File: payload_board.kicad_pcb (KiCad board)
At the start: 4 copper layers, 100 x 100 mm, 100 parts, among them IC1 RP2040_QFN56, IC2 AZ1117CH-3.3TRG1, J1 Cam_PicoLock, J10 503398-1892, J12 FC Breakout, J15 SWC, J2 Cam_Conn, J3 Antenna_Conn, J4 usb jumper, J5 Display_Conn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

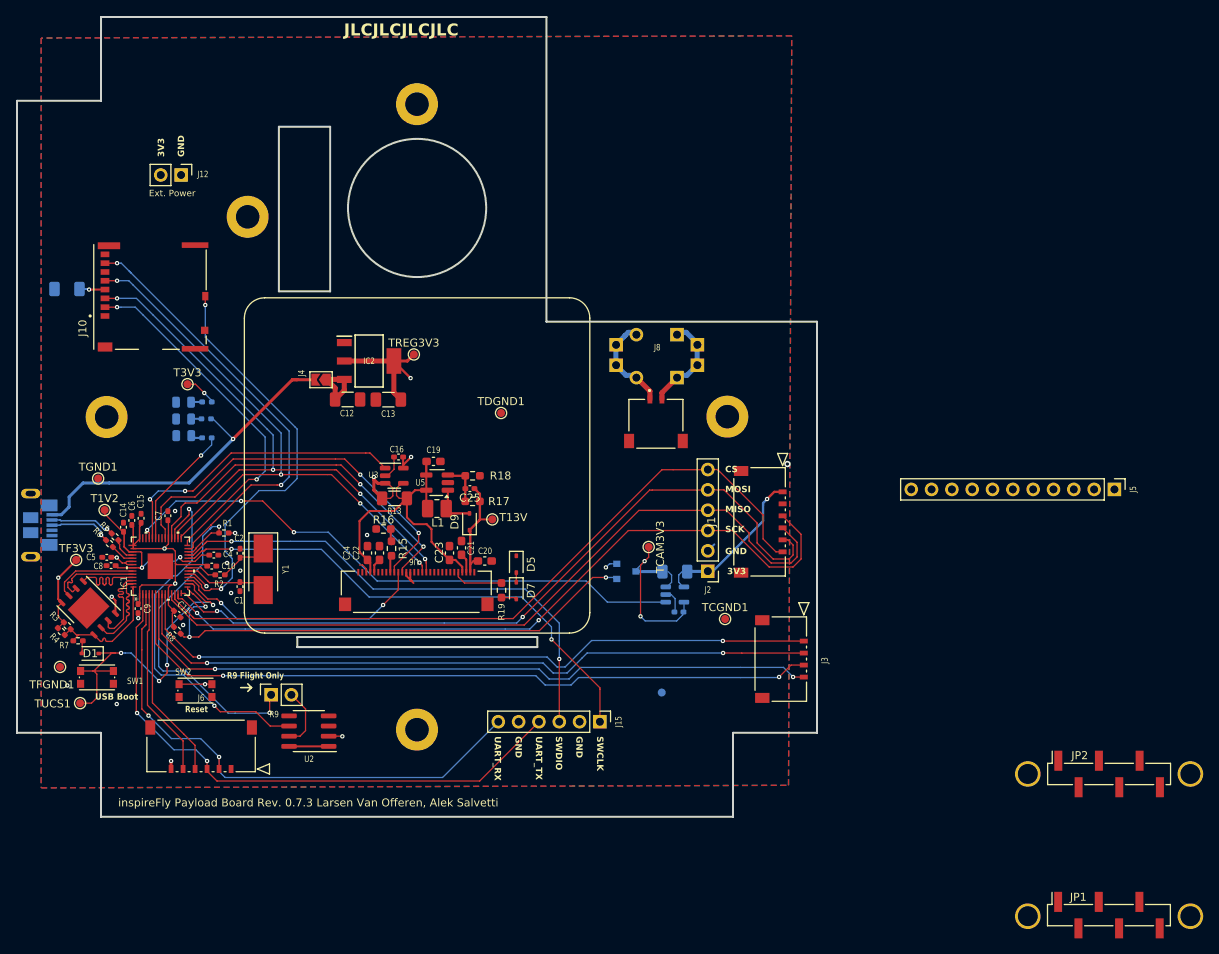
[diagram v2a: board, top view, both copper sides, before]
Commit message: Updated footprints to reduce part count.
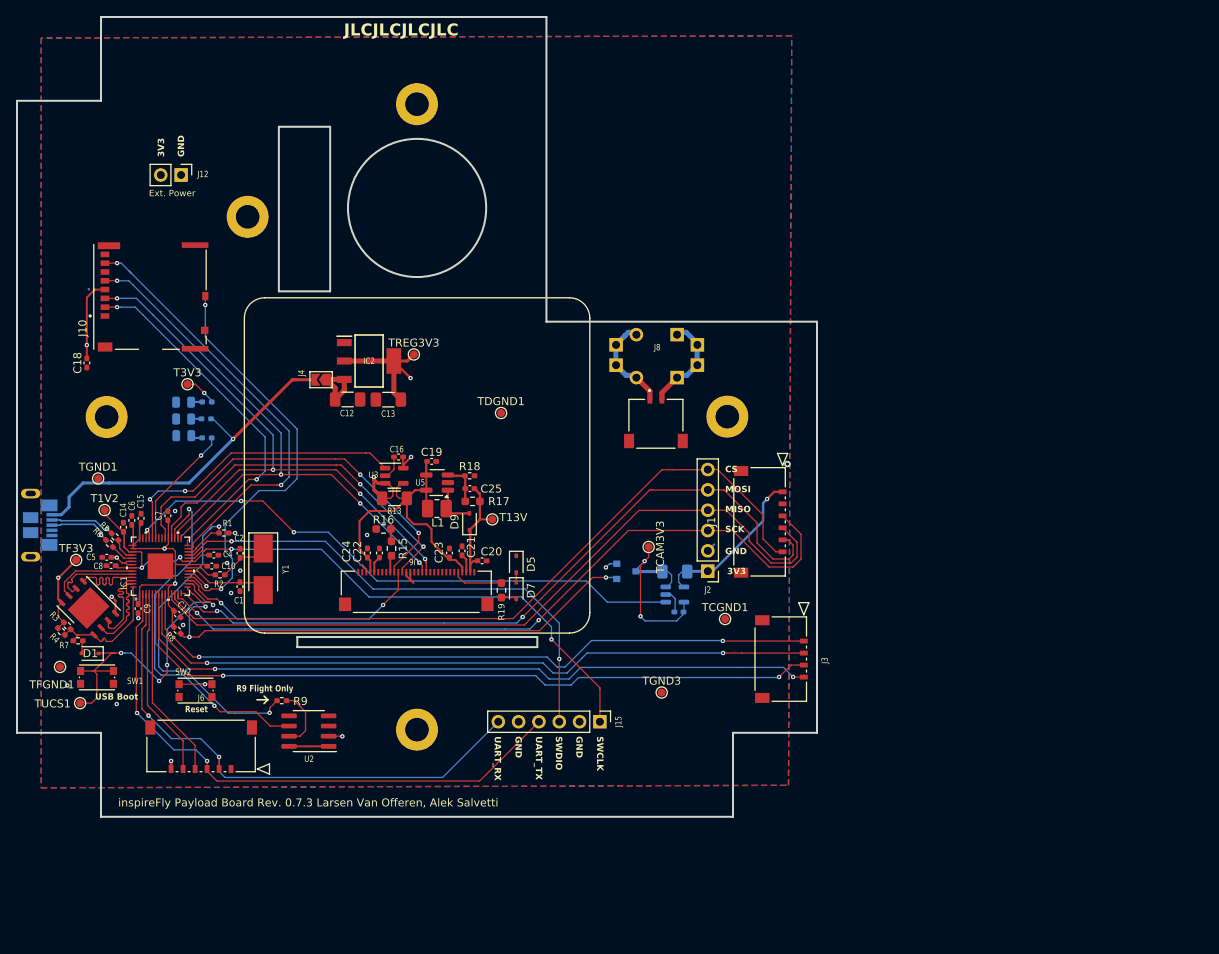
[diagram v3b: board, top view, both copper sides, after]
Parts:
- removed the ? at (159.7, 107.6)
- removed the ? at (139.3, 107.6)
- removed the ? at (159.7, 125.4)
- removed the ? at (139.3, 125.4)
- removed the J5 at (150.2, 72.0)
- removed JP1, JP2: , Connector_PinHeader_2.54mm:PinHeader_1x06_P2.54mm_Vertical_SMD_Pin1Right
- C18: footprint Capacitor_SMD:C_1206_3216Metric_Pad1.33x1.80mm_HandSolder -> Capacitor_SMD:C_0402_1005Metric_Pad0.74x0.62mm_HandSolder; moved to F.Cu
- C19, C20, C21, C24: footprint Capacitor_SMD:C_0603_1608Metric_Pad1.08x0.95mm_HandSolder -> Capacitor_SMD:C_0402_1005Metric_Pad0.74x0.62mm_HandSolder
- C22, C23: value 1.0uF -> 1uF; footprint Capacitor_SMD:C_0603_1608Metric_Pad1.08x0.95mm_HandSolder -> Capacitor_SMD:C_0402_1005Metric_Pad0.74x0.62mm_HandSolder
- R1: value 10K -> 10k
- R18: footprint Resistor_SMD:R_0603_1608Metric_Pad0.98x0.95mm_HandSolder -> Resistor_SMD:R_0402_1005Metric_Pad0.72x0.64mm_HandSolder
- R9: footprint Connector_PinSocket_2.54mm:PinSocket_1x02_P2.54mm_Vertical -> Resistor_SMD:R_0402_1005Metric_Pad0.72x0.64mm_HandSolder
- TGND3: moved to F.Cu
- moved C18 9.57 mm to (21.7, 56.2), turned to 90 degrees
- moved R9 1.53 mm to (46.1, 98.5), turned to 0 degrees
- moved C21 0.37 mm to (68.6, 79.7)
- moved R18 0.36 mm to (69.6, 70.3)
- moved C20 0.34 mm to (71.1, 81.0)
- moved C19 0.23 mm to (64.8, 68.5)
- turned TGND3 to 0 degrees
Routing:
- net +3.3V: track 92.3 -> 99.7 mm
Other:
- board text removed: "Keep Together. Mounting for IMU"

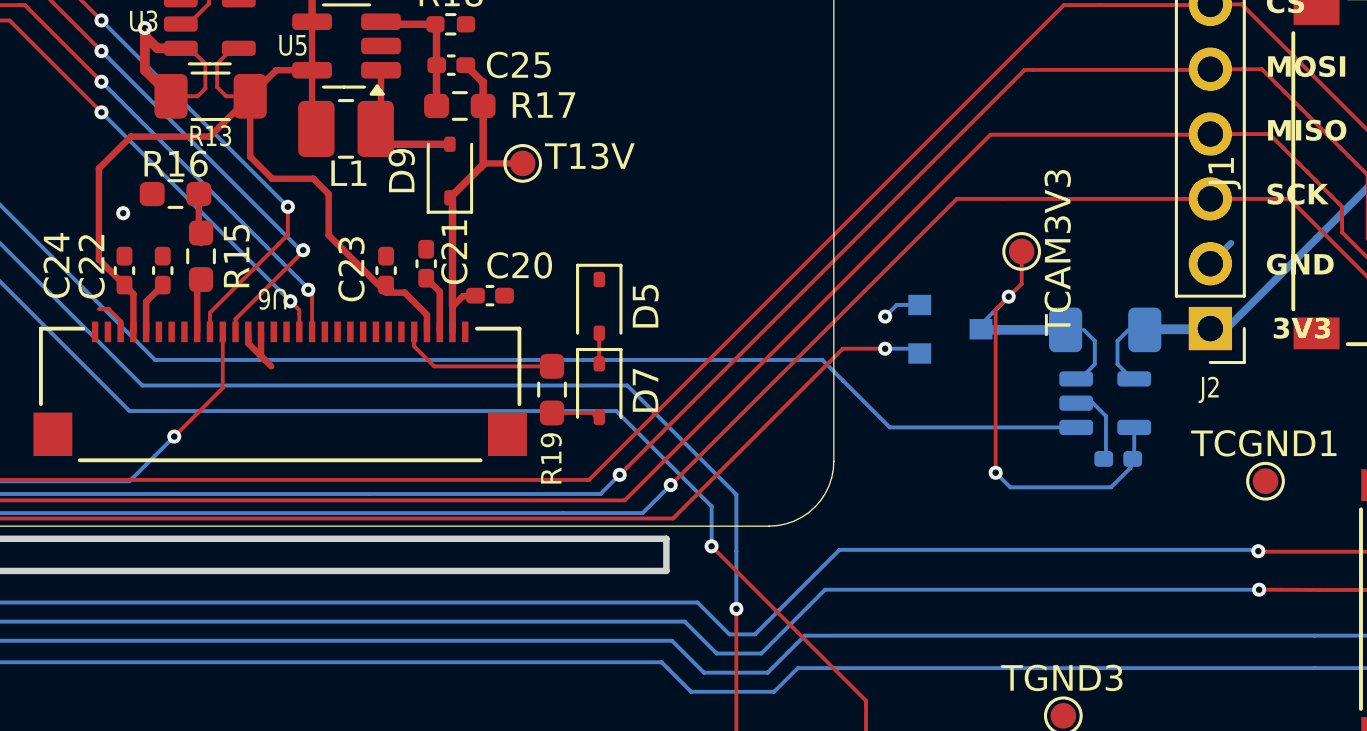
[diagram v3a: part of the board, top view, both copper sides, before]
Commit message: flipped camera power monitor and reset
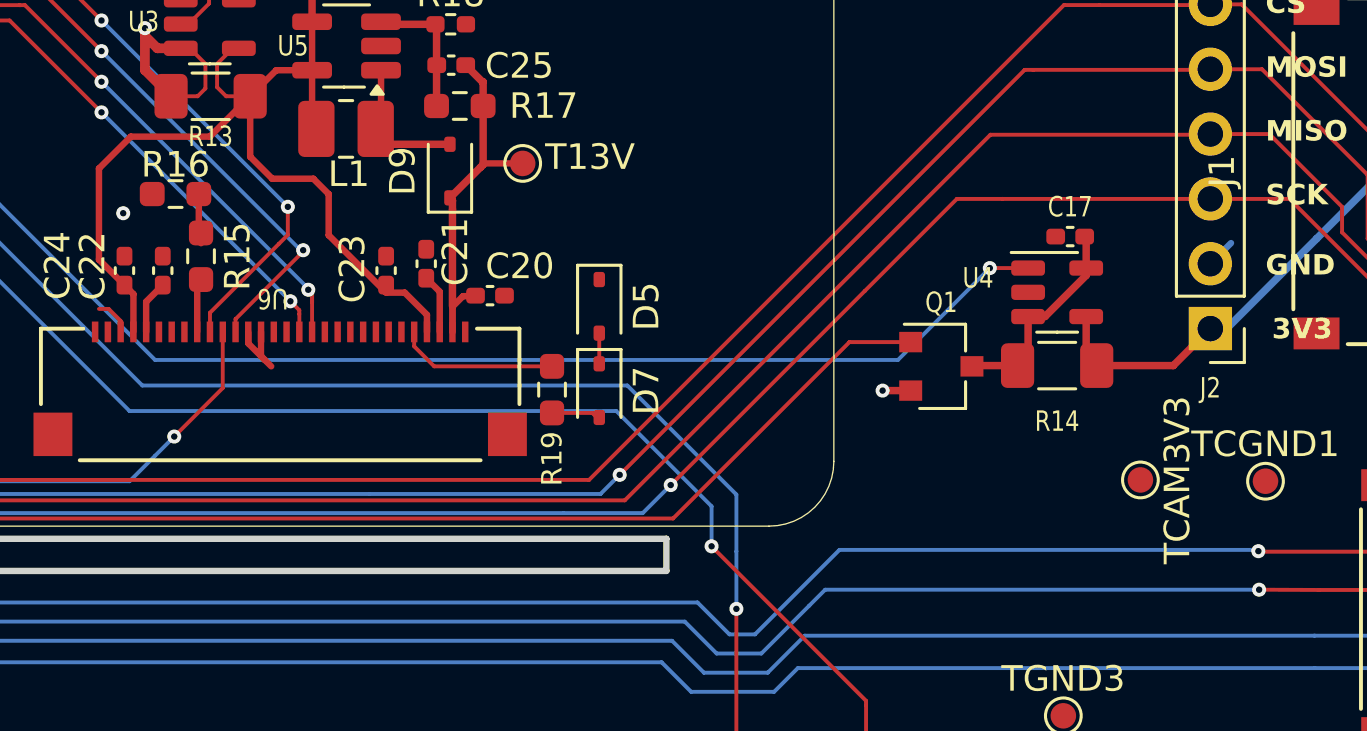
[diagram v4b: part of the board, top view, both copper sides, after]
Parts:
- C17, Q1, R14, U4: moved to F.Cu
- moved TCAM3V3 10.1 mm to (96.6, 88.2)
- moved C17 8.91 mm to (93.8, 78.7)
- moved U4 4.73 mm to (93.3, 80.8)
- moved R14 2.35 mm to (93.3, 83.7)
- moved Q1 1.50 mm to (88.8, 83.8)
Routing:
- net Cam_3.3v: track 23.8 -> 8.38 mm, vias 2 -> 0
- net GND: track 16.8 -> 13.8 mm
- net CIN-: track 19.4 -> 21.9 mm
- net ADC1: track 72.8 -> 71.3 mm, vias 3 -> 4
- net Cam_RST: track 66.8 -> 66.5 mm, vias 3 -> 2

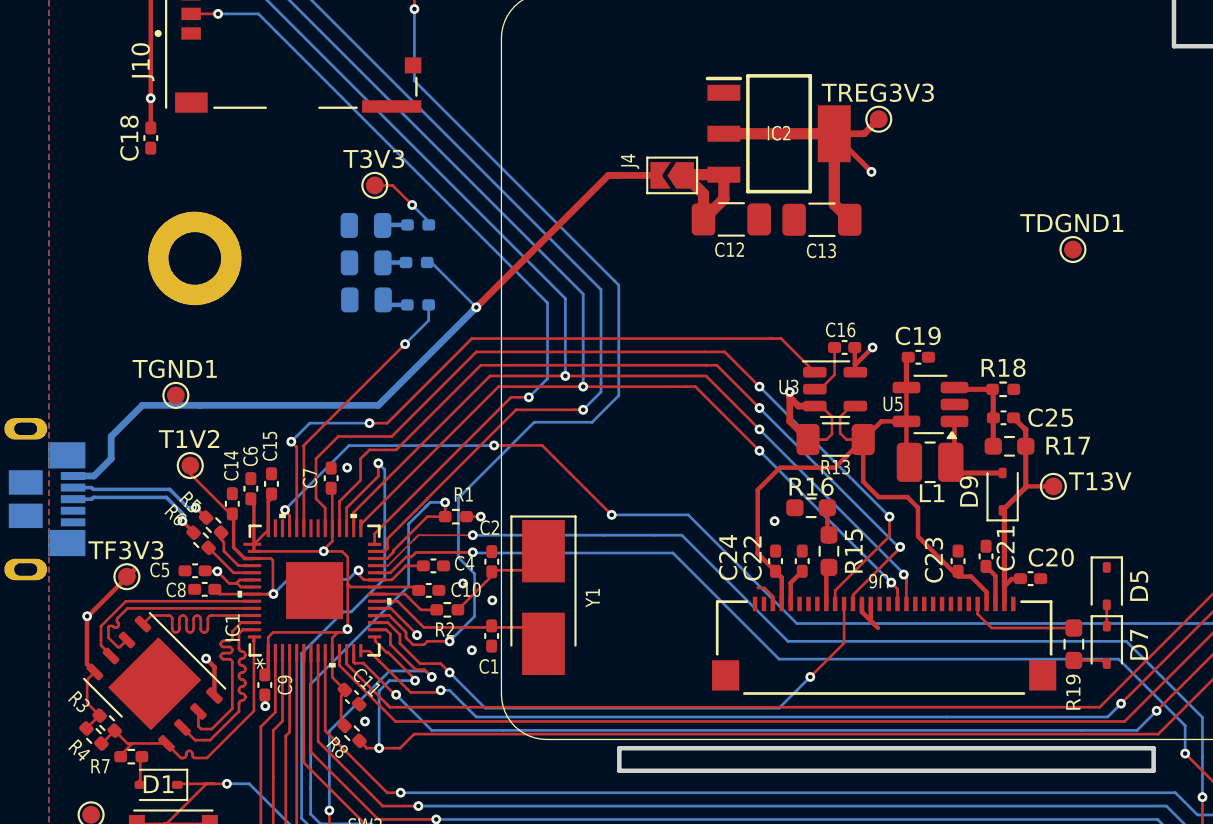
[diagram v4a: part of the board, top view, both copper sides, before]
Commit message: Update for JLC PCBA part selection
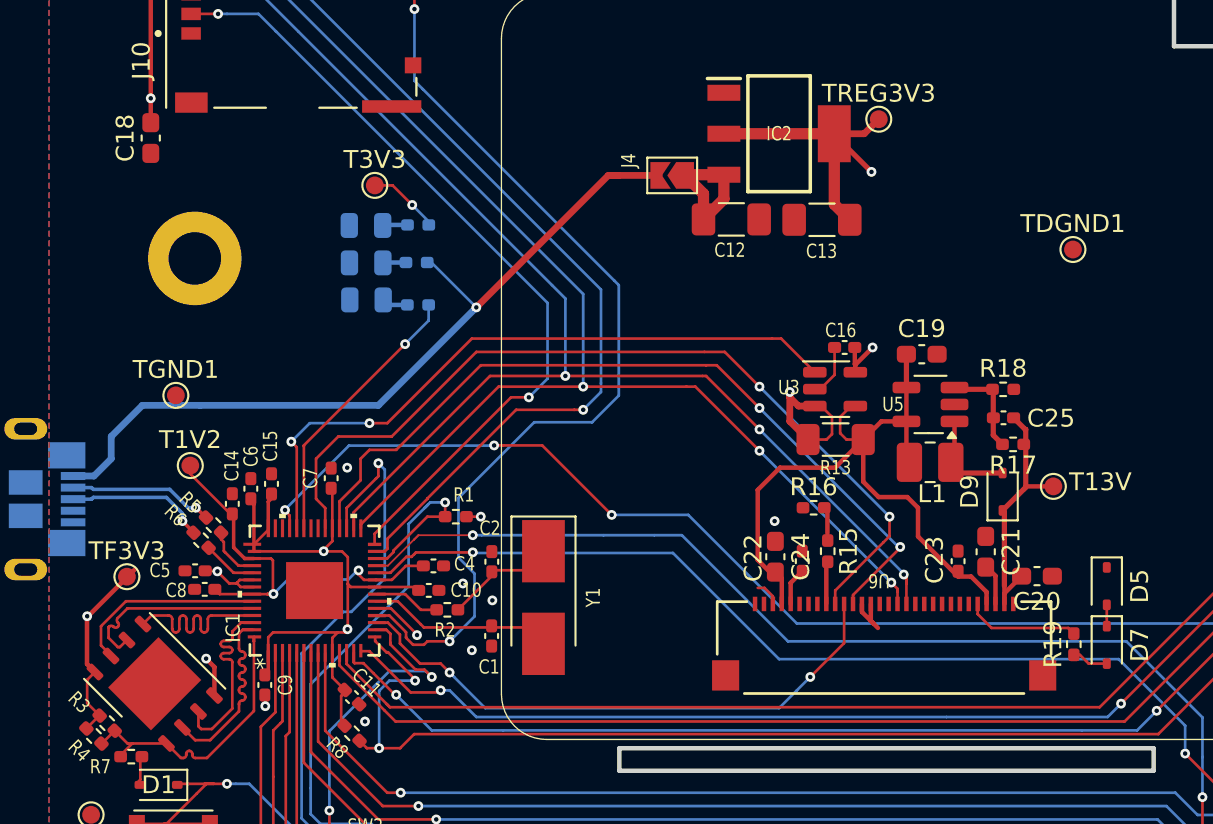
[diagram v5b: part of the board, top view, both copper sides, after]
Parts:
- C18, C19, C20, C21, C24: footprint Capacitor_SMD:C_0402_1005Metric_Pad0.74x0.62mm_HandSolder -> Capacitor_SMD:C_0603_1608Metric_Pad1.08x0.95mm_HandSolder
- R14: value 10k -> 0.065
- R15, R16, R17, R19: footprint Resistor_SMD:R_0603_1608Metric_Pad0.98x0.95mm_HandSolder -> Resistor_SMD:R_0402_1005Metric_Pad0.72x0.64mm_HandSolder
- moved C20 0.39 mm to (71.5, 80.8)
- moved C21 0.26 mm to (68.6, 79.5)
- moved C19 0.25 mm to (65.0, 68.4)
- moved C24 0.25 mm to (56.8, 79.8)
- moved R17 0.23 mm to (70.1, 73.4)
- moved R16 0.14 mm to (58.9, 77.0)
- moved R15 0.07 mm to (59.7, 79.4)
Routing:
- net DIN-: track 39.7 -> 40.3 mm

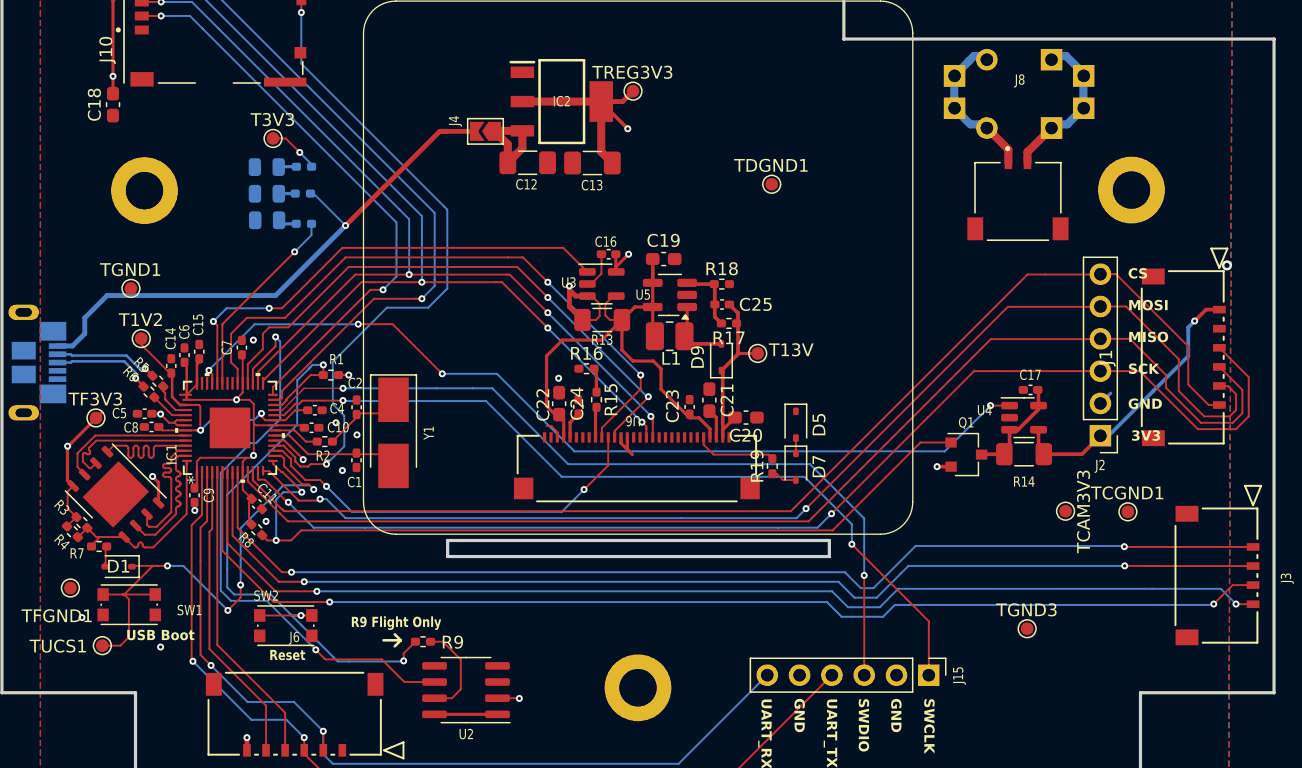
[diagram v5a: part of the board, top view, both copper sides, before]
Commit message: Added new 13V boost converter
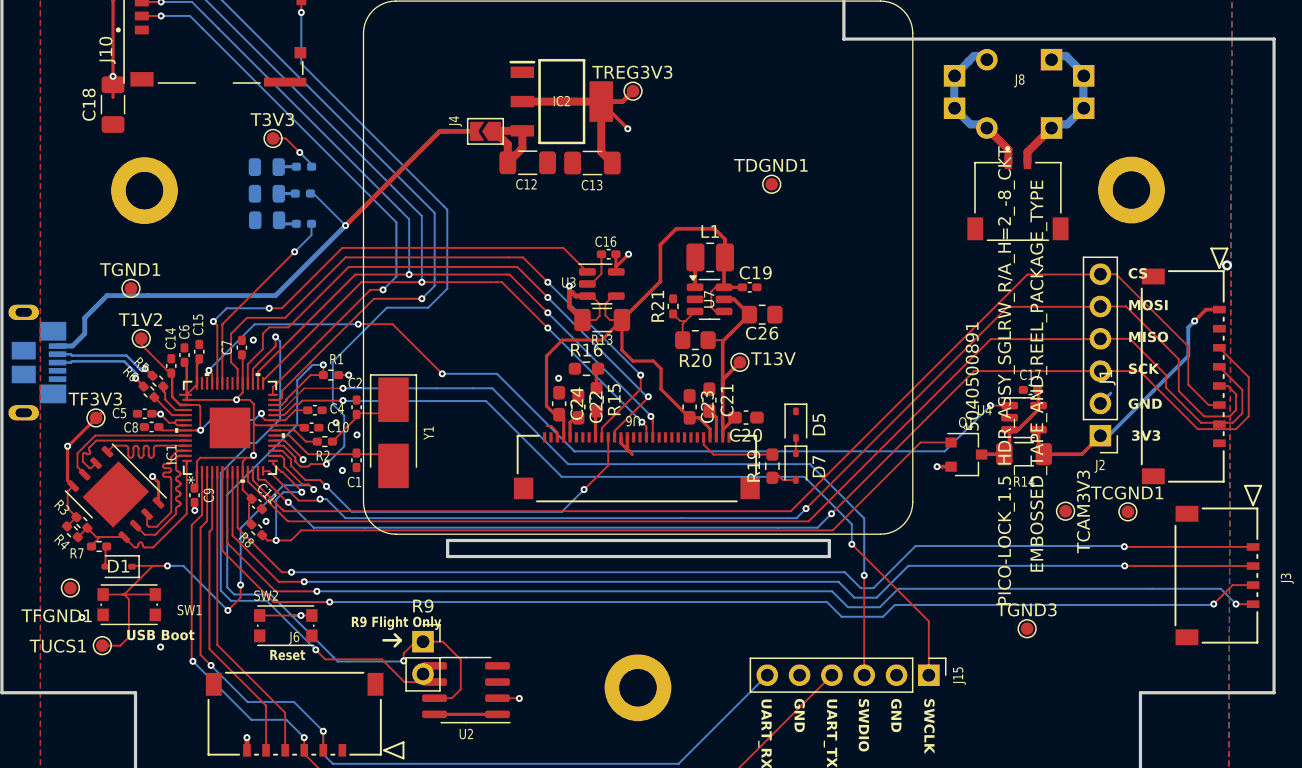
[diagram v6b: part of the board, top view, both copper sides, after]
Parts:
- removed C25: 0.1uF, Capacitor_SMD:C_0402_1005Metric_Pad0.74x0.62mm_HandSolder
- removed D9: NSR0320, Diode_SMD:D_SOD-323
- removed R17: 100k, Resistor_SMD:R_0402_1005Metric_Pad0.72x0.64mm_HandSolder
- removed R18: 10k, Resistor_SMD:R_0402_1005Metric_Pad0.72x0.64mm_HandSolder
- removed U5: FAN5331SX, Package_TO_SOT_SMD:SOT-23-5_HandSoldering
- added C26: 4.7uF, Resistor_SMD:R_0805_2012Metric_Pad1.20x1.40mm_HandSolder, F.Cu at (72.8, 72.8)
- added R20: 16k, Resistor_SMD:R_0805_2012Metric_Pad1.20x1.40mm_HandSolder, F.Cu at (67.5, 74.8)
- added R21: 1k, Resistor_SMD:R_0402_1005Metric_Pad0.72x0.64mm_HandSolder, F.Cu at (65.8, 72.1)
- added U7: TLV61046ADB, Package_TO_SOT_SMD:SOT-23-6, F.Cu at (68.6, 71.5)
- C18: footprint Capacitor_SMD:C_0603_1608Metric_Pad1.08x0.95mm_HandSolder -> Capacitor_SMD:C_1206_3216Metric_Pad1.33x1.80mm_HandSolder
- C19: value 10uF -> 1uF; footprint Capacitor_SMD:C_0603_1608Metric_Pad1.08x0.95mm_HandSolder -> Capacitor_SMD:C_0402_1005Metric_Pad0.74x0.62mm_HandSolder
- C22, C23: value 1uF -> 1.0uF; footprint Capacitor_SMD:C_0402_1005Metric_Pad0.74x0.62mm_HandSolder -> Capacitor_SMD:C_0603_1608Metric_Pad1.08x0.95mm_HandSolder
- J1: footprint PayloadBoard:Molex_Pico_CON_5040500691 -> PayloadBoard:Molex_Pico_CON_5040500891
- R15, R16, R19: footprint Resistor_SMD:R_0402_1005Metric_Pad0.72x0.64mm_HandSolder -> Resistor_SMD:R_0603_1608Metric_Pad0.98x0.95mm_HandSolder
- R9: footprint Resistor_SMD:R_0402_1005Metric_Pad0.72x0.64mm_HandSolder -> Connector_PinSocket_2.54mm:PinSocket_1x02_P2.54mm_Vertical
- moved C19 7.11 mm to (71.8, 70.6), turned to 180 degrees
- moved L1 6.97 mm to (68.7, 68.2), turned to 180 degrees
- moved T13V 1.57 mm to (71.0, 76.5)
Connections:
- C19 pad 1: DIN- -> GND
- C19 pad 2: GND -> DIN-
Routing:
- net DIN-: track 40.3 -> 52.9 mm
- net Net-(U5-FB): track 5.52 -> 0.00 mm
- net +13V: track 15.2 -> 19.6 mm
- net Net-(U7-FB): track 0.00 -> 3.86 mm
- net Net-(U7-SW): track 5.54 -> 2.36 mm
